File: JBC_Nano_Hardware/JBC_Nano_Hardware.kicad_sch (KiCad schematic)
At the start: 47 parts, among them J1 POWER_IN, J2 IRON, J3 PROG, J4 UART, J5 Display128x32, Q1 FDS9435A, SW1 Rotary_Encoder_Switch, SW2 RESET, SW3 BOOT, U1 STM32F030F4Px, U2 AP1117-33, U4 AD8615, U5 UCC2751, U6 AT24CS01-STUM, Y1 Crystal_GND24

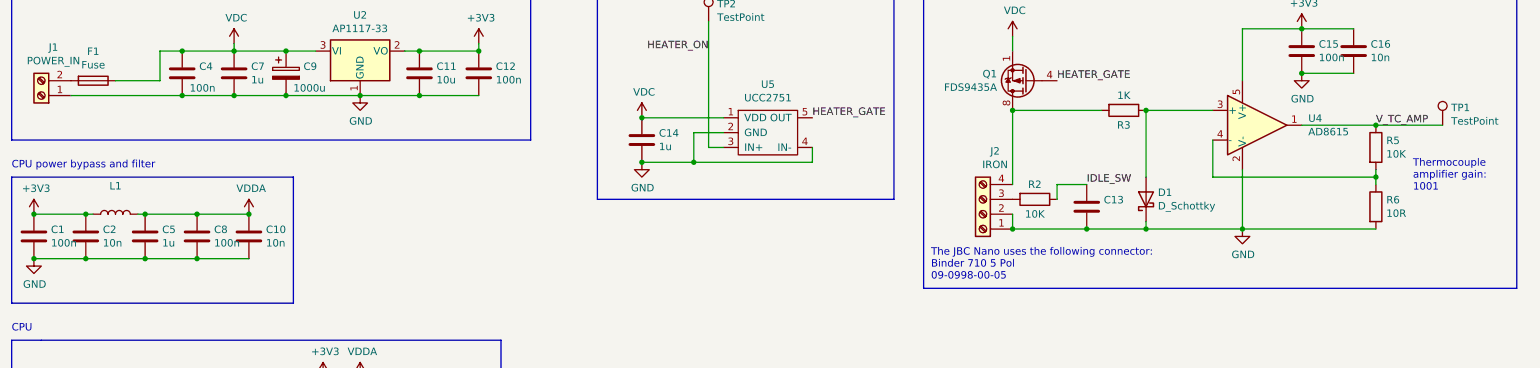
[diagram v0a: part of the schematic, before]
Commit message: Fixed wrong resistor value for thermocouple gain
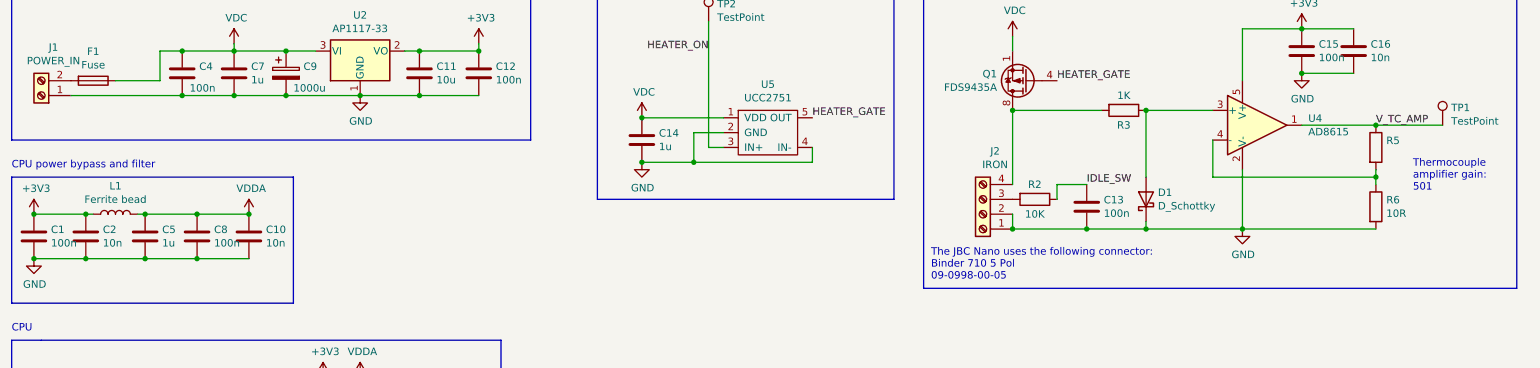
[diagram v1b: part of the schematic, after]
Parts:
- C13: value (none) -> 100n
- L1: value (none) -> Ferrite bead
- R5: value 10K -> (none)
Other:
- note added: "Thermocouple amplifier gain: 501"
- note removed: "Thermocouple amplifier gain: 1001"
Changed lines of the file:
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@@
     (effects (font (size 1.27 1.27)) (justify left bottom))
   )
-  (text "Thermocouple\namplifier gain:\n1001" (at 257.81 55.88 0)
+  (text "Thermocouple\namplifier gain:\n501" (at 257.81 55.88 0)
     (effects (font (size 1.27 1.27)) (justify left bottom))
   )
@@
       (effects (font (size 1.27 1.27)) (justify left))
     )
-    (property "Value" "10K" (id 1) (at 253.238 49.403 0)
+    (property "Value" "" (id 1) (at 253.238 49.403 0)
       (effects (font (size 1.27 1.27)) (justify left))
     )
@@
     (in_bom yes) (on_board yes)
     (property "Reference" "L1" (id 0) (at 35.56 54.864 90))
-    (property "Value" "" (id 1) (at 35.56 57.1754 90))
+    (property "Value" "Ferrite bead" (id 1) (at 35.56 57.1754 90))
     (property "Footprint" "Inductor_SMD:L_0805_2012Metric" (id 2) (at 35.56 59.69 0)
       (effects (font (size 1.27 1.27)) hide)
@@
       (effects (font (size 1.27 1.27)) (justify left))
     )
-    (property "Value" "" (id 1) (at 204.851 59.563 0)
+    (property "Value" "100n" (id 1) (at 204.851 59.563 0)
       (effects (font (size 1.27 1.27)) (justify left))
     )
@@
     )
     (path "/00000000-0000-0000-0000-00005f4a9714"
-      (reference "R5") (unit 1) (value "10K") (footprint "Resistor_SMD:R_0603_1608Metric")
+      (reference "R5") (unit 1) (value "5K") (footprint "Resistor_SMD:R_0603_1608Metric")
     )
     (path "/00000000-0000-0000-0000-00005f4aa0b0"
